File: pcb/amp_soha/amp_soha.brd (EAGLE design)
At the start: 90.2 x 48.9 mm, 59 parts, among them IC1 NE5535U, IC2 7812, IC3 7912, Q1 J113, Q2 J113, Q3 J113, Q4 J113

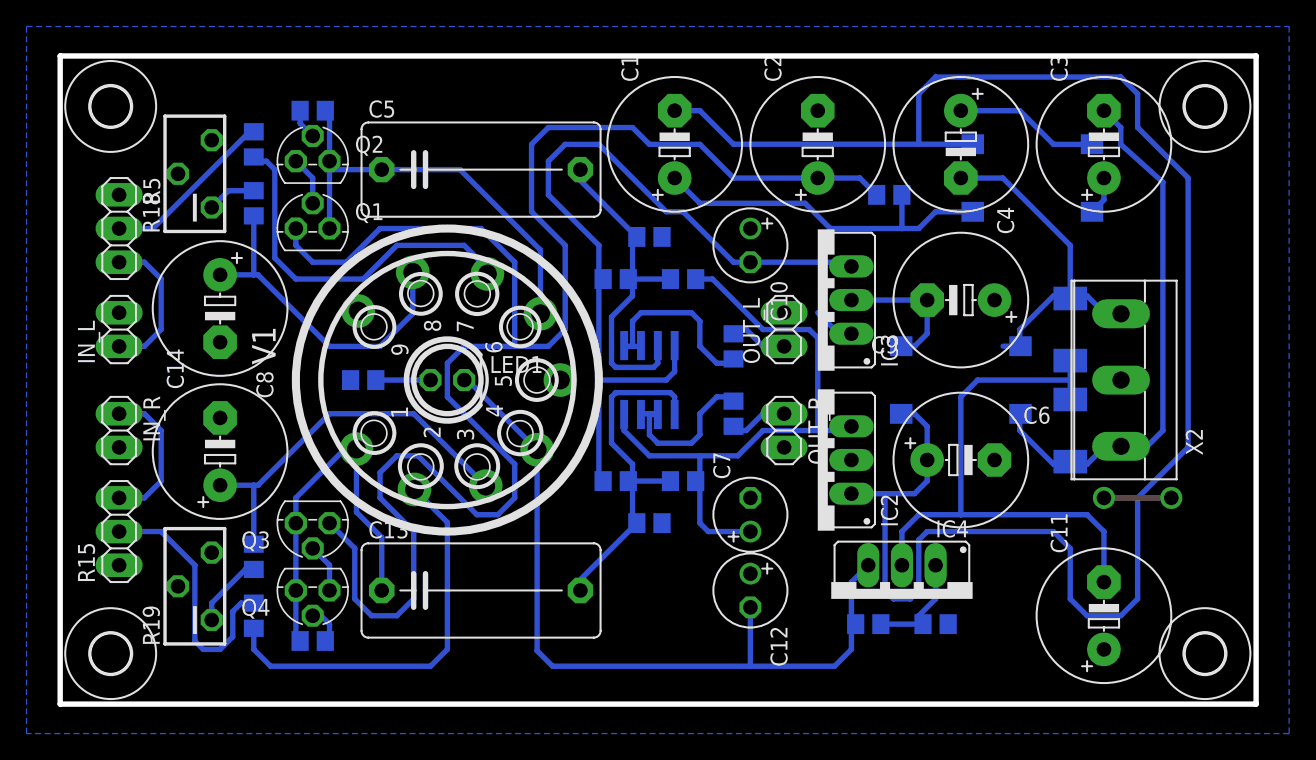
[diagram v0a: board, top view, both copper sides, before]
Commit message: 
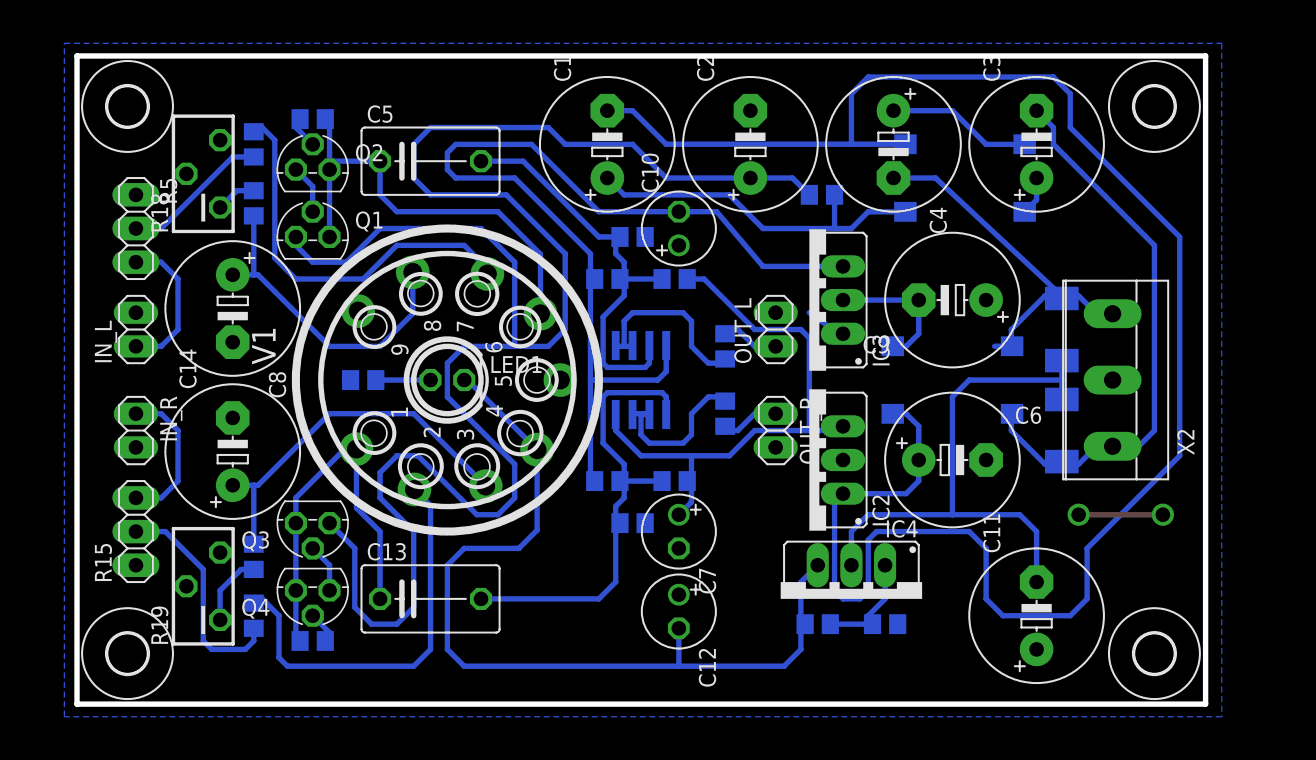
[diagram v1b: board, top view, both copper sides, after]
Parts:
- C13, C5: device amp_soha:C150-072X183 -> amp_soha:C075-052X106
- moved C12 5.63 mm to (46.7, 7.94)
- moved C10 5.54 mm to (46.7, 36.8), turned to 90 degrees
- moved C7 5.54 mm to (46.7, 14.0), turned to 270 degrees
- moved B1 5.08 mm to (68.3, 40.6)
- moved C1 5.08 mm to (41.3, 43.2)
- moved C11 5.08 mm to (73.7, 7.62)
- moved C2 5.08 mm to (52.1, 43.2)
- moved C3 5.08 mm to (73.7, 43.2)
- moved R1 5.08 mm to (57.5, 39.4)
- moved C4 5.08 mm to (62.9, 43.2)
- moved C13 3.86 mm to (27.9, 8.89)
- moved C5 3.86 mm to (27.9, 41.9)
- moved R11 3.81 mm to (62.2, 6.99)
- moved IC4 3.81 mm to (59.7, 8.89)
- moved R9 3.81 mm to (57.1, 6.99)
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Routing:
- net -12V: track 61.4 -> 74.5 mm
- net +24V: track 128.3 -> 139.8 mm
- net N$34: track 27.0 -> 35.7 mm
- net -12.6V: track 59.1 -> 65.7 mm
- net N$22: track 27.3 -> 33.6 mm
- net N$6: track 135.1 -> 138.9 mm
- net +12V: track 48.3 -> 44.6 mm
- net N$27: track 19.8 -> 17.0 mm
- net N$14: track 27.5 -> 29.9 mm
- net N$13: track 13.2 -> 11.1 mm
- net N$2: track 26.6 -> 28.4 mm
- net N$1: track 40.5 -> 42.3 mm
- net N$19: track 32.4 -> 33.8 mm
- net N$3: track 43.2 -> 42.0 mm
- net AGND: track 8.28 -> 9.40 mm
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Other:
- board size 90.2 x 48.9 mm -> 85.1 x 48.9 mm
